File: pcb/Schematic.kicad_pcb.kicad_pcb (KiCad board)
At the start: 2 copper layers, 85.7 x 69.6 mm, 22 parts, among them SW1 SW_Push, SW2 SW_Push, SW3 SW_Push, SW4 SW_Push, SW5 SW_Push, SW6 SW_Push, SW7 RotaryEncoder_Switch, SW8 SW_Push, U1 XIAO-RP2040-DIP

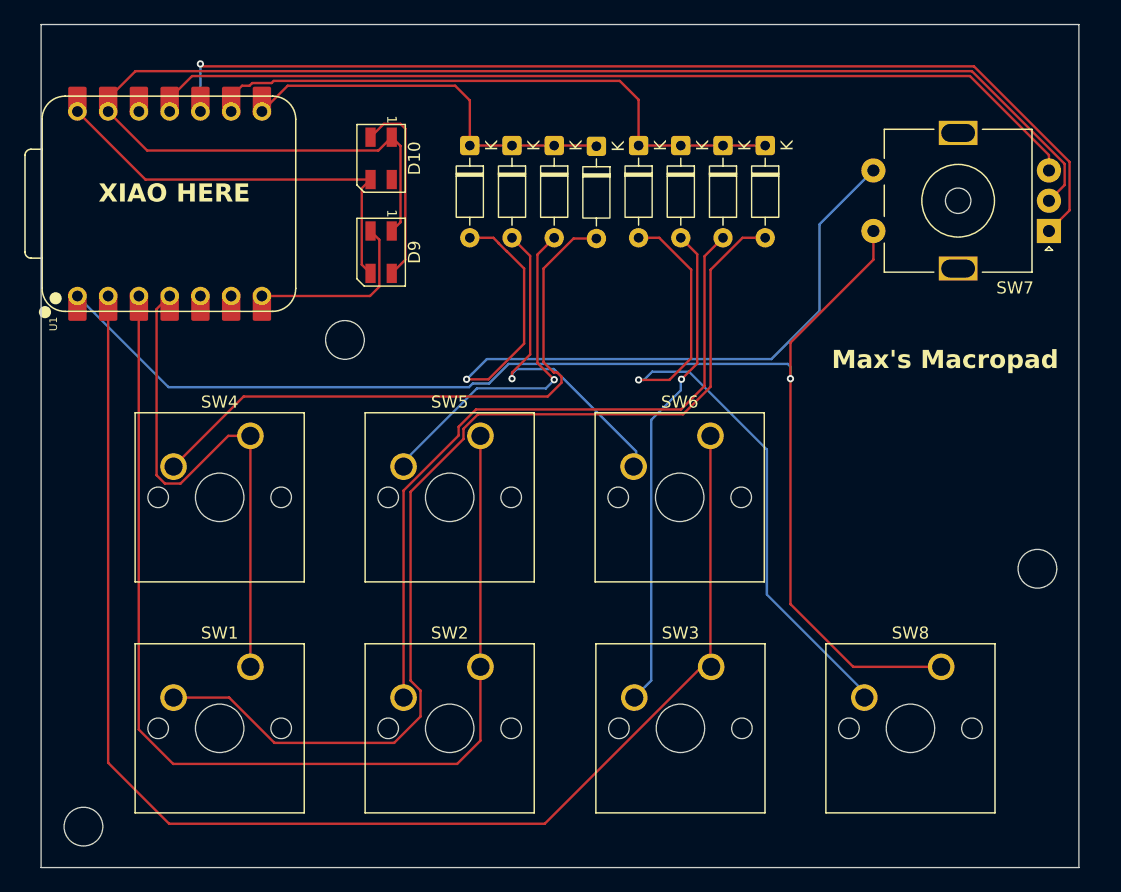
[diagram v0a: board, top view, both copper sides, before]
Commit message: new leds
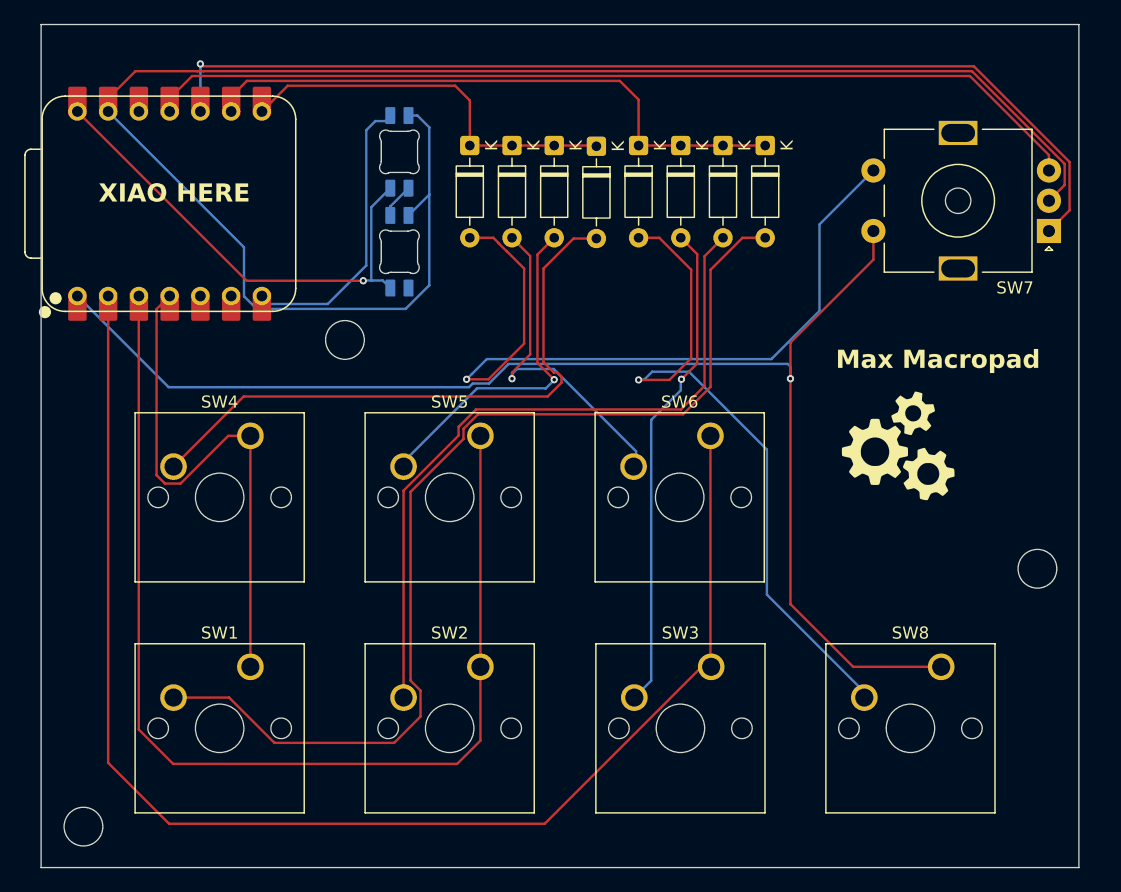
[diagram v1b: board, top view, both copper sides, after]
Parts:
- added G***: LOGO, LOGO, F.Cu at (88.8, 49.8)
- D10, D9: value SK6812 -> SK6812MINI; footprint LED_SMD:LED_SK6812MINI_PLCC4_3.5x3.5mm_P1.75mm -> Meine_Bauteile:MX_SK6812MINI-E_REV
- moved D9 10.6 mm to (52.7, 25.5)
- moved D10 10.1 mm to (52.7, 33.7)
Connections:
- D10 pad 1: GND -> unconnected-(D10-DOUT-Pad1)
- D10 pad 2: Net-(D10-DIN) -> GND
- D10 pad 3: +5V -> Net-(D10-DIN)
- D10 pad 4: unconnected-(D10-DOUT-Pad4) -> +5V
- D9 pad 1: GND -> Net-(D10-DIN)
- D9 pad 2: Net-(D9-DIN) -> GND
- D9 pad 3: +5V -> Net-(D9-DIN)
- D9 pad 4: Net-(D10-DIN) -> +5V
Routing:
- net GND: track 121.3 -> 141.8 mm
- net Net-(D10-DIN): track 15.9 -> 2.87 mm
- net Net-(D9-DIN): track 14.9 -> 23.9 mm
- net +5V: track 34.9 -> 40.2 mm, vias 0 -> 1
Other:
- board text added: "Max Macropad"
- board text removed: "Max's Macropad"

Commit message: new pcb (clean up)
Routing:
- net Net-(D1-K): track 50.3 -> 49.1 mm
- net Net-(U1-GPIO3/MOSI): track 78.5 -> 77.4 mm
- net Net-(U1-GPIO29/ADC3/A3): track 45.1 -> 44.0 mm
- net GND: track 141.8 -> 140.8 mm
- net Net-(U1-GPIO27/ADC1/A1): track 114.9 -> 114.1 mm
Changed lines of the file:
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@@
 			(drillshape 0)
 			(scaleselection 1)
-			(outputdirectory "../Max-Macropad/prod/gerbers/")
+			(outputdirectory "../gerbers/")
 		)
 	)
@@
 	)
 	(segment
-		(start 33.7 20.9)
-		(end 33.7 22.13)
-		(width 0.2)
-		(layer "F.Cu")
-		(net 1)
-	)
-	(segment
 		(start 65.8 19.6)
 		(end 35 19.6)
@@
 	)
 	(segment
-		(start 48.16 70.32)
-		(end 47.94 70.54)
-		(width 0.2)
-		(layer "F.Cu")
-		(net 3)
-	)
-	(segment
 		(start 72.2 33.918929)
 		(end 70.841071 32.56)
@@
 	)
 	(segment
-		(start 53.54 24.94)
-		(end 53.7 25.1)
-		(width 0.2)
-		(layer "F.Cu")
-		(net 6)
-	)
-	(segment
 		(start 53.4125 24.94)
 		(end 56.898214 24.94)
@@
 	)
 	(segment
-		(start 63.809643 24.94)
-		(end 63.869643 25)
-		(width 0.2)
-		(layer "F.Cu")
-		(net 6)
-	)
-	(segment
-		(start 53.4125 24.94)
-		(end 53.54 24.94)
-		(width 0.2)
-		(layer "F.Cu")
-		(net 6)
-	)
-	(segment
 		(start 52.2 20)
 		(end 38.37 20)
@@
 	)
 	(segment
-		(start 46.8475 22.4625)
-		(end 46.8475 22.5175)
-		(width 0.2)
-		(layer "B.Cu")
-		(net 11)
-	)
-	(segment
 		(start 44.86 23.67)
 		(end 44.86 34.85)
@@
 	)
 	(segment
-		(start 23.54 22.13)
-		(end 23.54 21.05237)
-		(width 0.2)
-		(layer "F.Cu")
-		(net 12)
-	)
-	(segment
 		(start 30.910057 18.798)
 		(end 30.911057 18.799)
@@
 	)
 	(segment
-		(start 28.62 38.44763)
-		(end 28.62 37.37)
-		(width 0.2)
-		(layer "F.Cu")
-		(net 14)
-	)
-	(segment
 		(start 27.539 52.17053)
 		(end 27.539 38.451)
@@
 	)
 	(segment
-		(start 25.95275 37.49725)
-		(end 26.08 37.37)
-		(width 0.2)
-		(layer "F.Cu")
-		(net 15)
-	)
-	(segment
 		(start 54.29 74.1)
 		(end 54.29 68)
@@
 	)
 	(segment
-		(start 26.08 37.37)
-		(end 26.068 37.382)
-		(width 0.2)
-		(layer "F.Cu")
-		(net 15)
-	)
-	(segment
-		(start 73.35 68)
-		(end 72.565184 68)
-		(width 0.2)
-		(layer "F.Cu")
-		(net 16)
-	)
-	(segment
 		(start 28.575 80.9625)
 		(end 23.54 75.9275)
@@
 	)
 	(segment
-		(start 73.29 67.94)
-		(end 73.35 68)
-		(width 0.2)
-		(layer "F.Cu")
-		(net 16)
-	)
-	(segment
 		(start 31.2 18.238)
 		(end 31.2 18.397)
@@
 		(width 0.2)
 		(layer "F.Cu")
-		(net 19)
-	)
-	(segment
-		(start 28.62 22.13)
-		(end 28.62 21.05237)
-		(width 0.2)
-		(layer "F.Cu")
